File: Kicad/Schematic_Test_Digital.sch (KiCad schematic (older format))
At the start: 71 parts, among them J301 I2C_CONNECTOR_OUT, J302 I2C_CONNECTOR_OUT, J303 CONN_JOYSTICK, J304 I2C_CONNECTOR_OUT, SW301 RESET PUSH, U301 TSX-3225, U302 MMC5603NJ, U303 LSM6DS33TR, U304 74HC595D, U305 74HC595D, U306 74HC595D

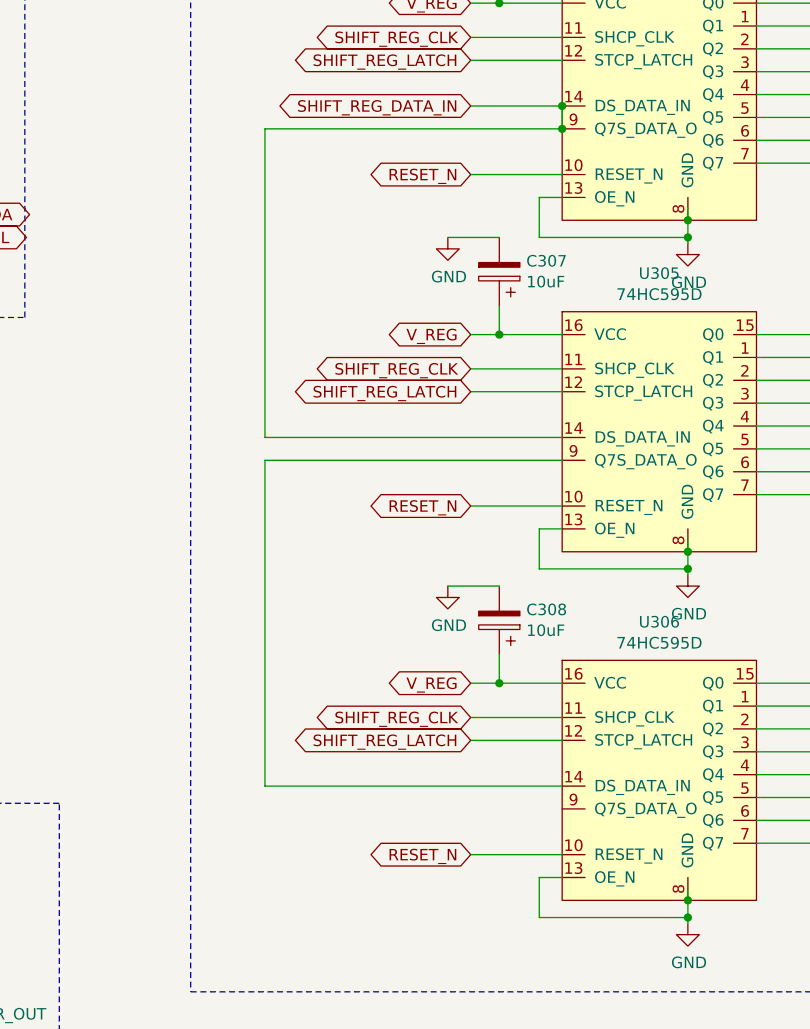
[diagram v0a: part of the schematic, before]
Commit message: Corrected some schematic labeling.
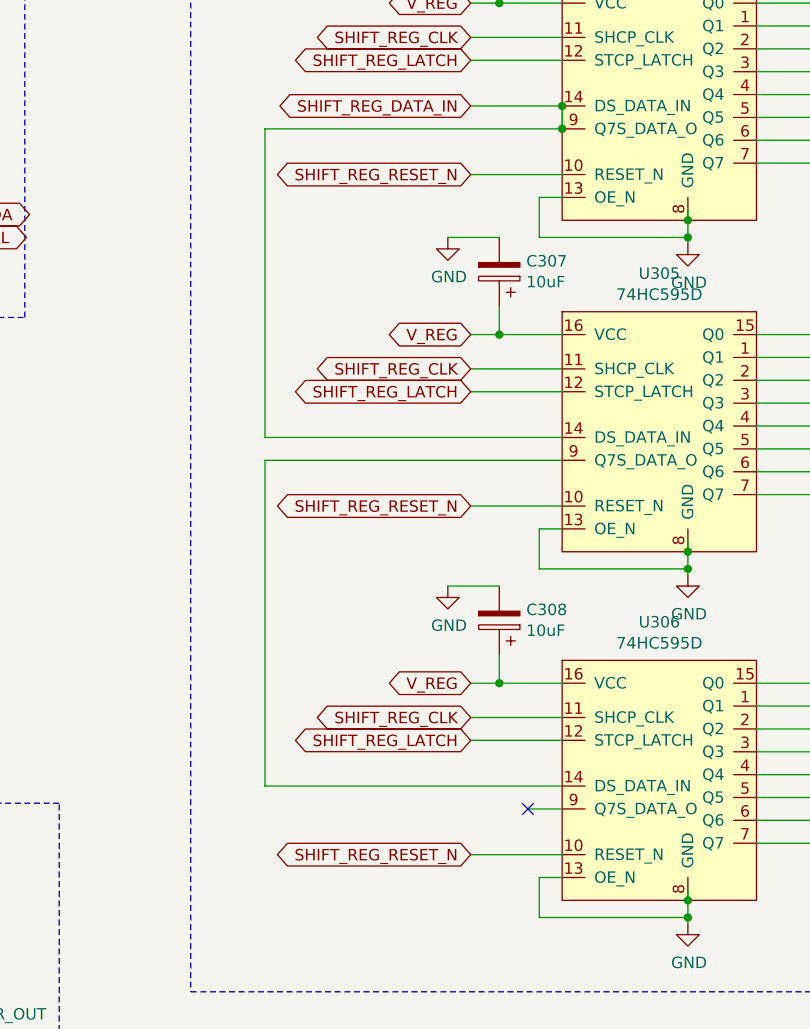
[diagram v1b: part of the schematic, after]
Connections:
- net RESET_N: no longer U304.10 (RESET_N), U305.10 (RESET_N), U306.10 (RESET_N)
- new net SHIFT_REG_RESET_N: U304.10 (RESET_N), U305.10 (RESET_N), U306.10 (RESET_N)
- no-connect marks 2 -> 3
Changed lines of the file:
@@
 Wire Wire Line
 	8700 4950 8300 4950
-Text GLabel 8300 4950 0    50   BiDi ~ 0
-RESET_N
 Wire Wire Line
 	9250 5100 9250 5150
@@
 Wire Wire Line
 	8700 3425 8300 3425
-Text GLabel 8300 3425 0    50   BiDi ~ 0
-RESET_N
 Wire Wire Line
 	9250 3575 9250 3625
@@
 Wire Wire Line
 	8300 1225 8425 1225
-Text GLabel 8300 1975 0    50   BiDi ~ 0
-RESET_N
 Text GLabel 8300 1225 0    50   BiDi ~ 0
 V_REG
@@
 Text GLabel 1800 1375 0    50   BiDi ~ 0
 RESET_N
+Text GLabel 8300 1975 0    50   BiDi ~ 0
+SHIFT_REG_RESET_N
+Text GLabel 8300 3425 0    50   BiDi ~ 0
+SHIFT_REG_RESET_N
+Text GLabel 8300 4950 0    50   BiDi ~ 0
+SHIFT_REG_RESET_N
+Wire Wire Line
+	8700 4750 8550 4750
+NoConn ~ 8550 4750
 $EndSCHEMATC

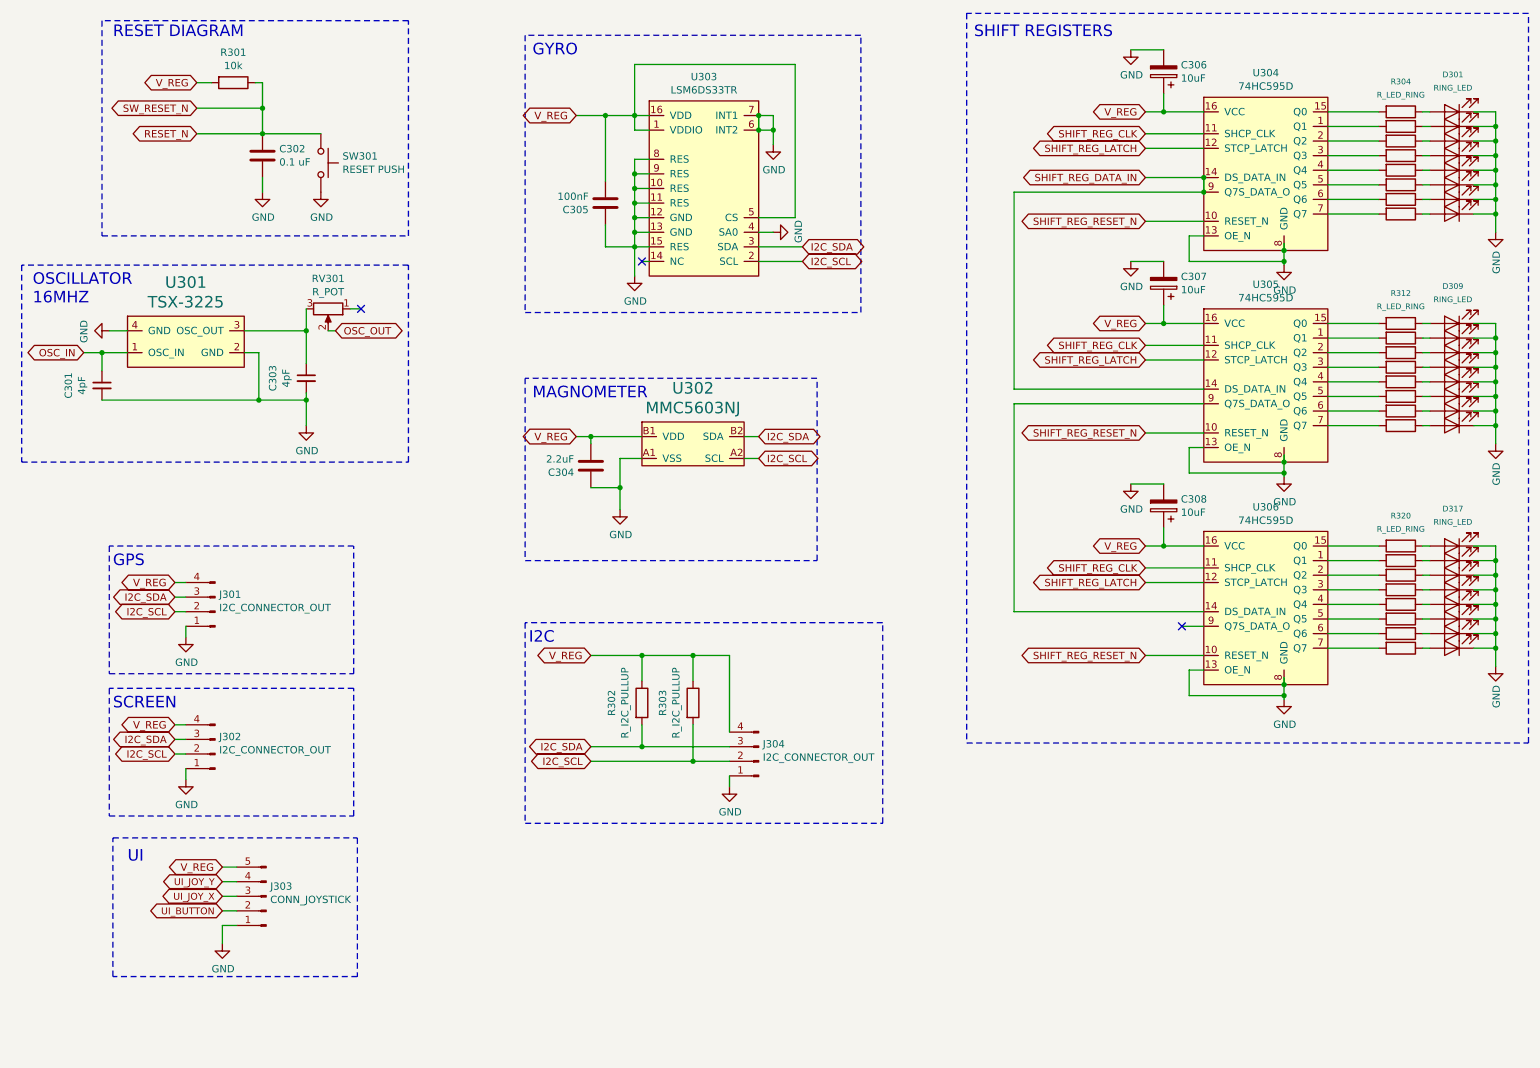
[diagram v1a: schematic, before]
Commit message: Assigned footprints to majority of refs. Missing is i2c due to unknown trace length.
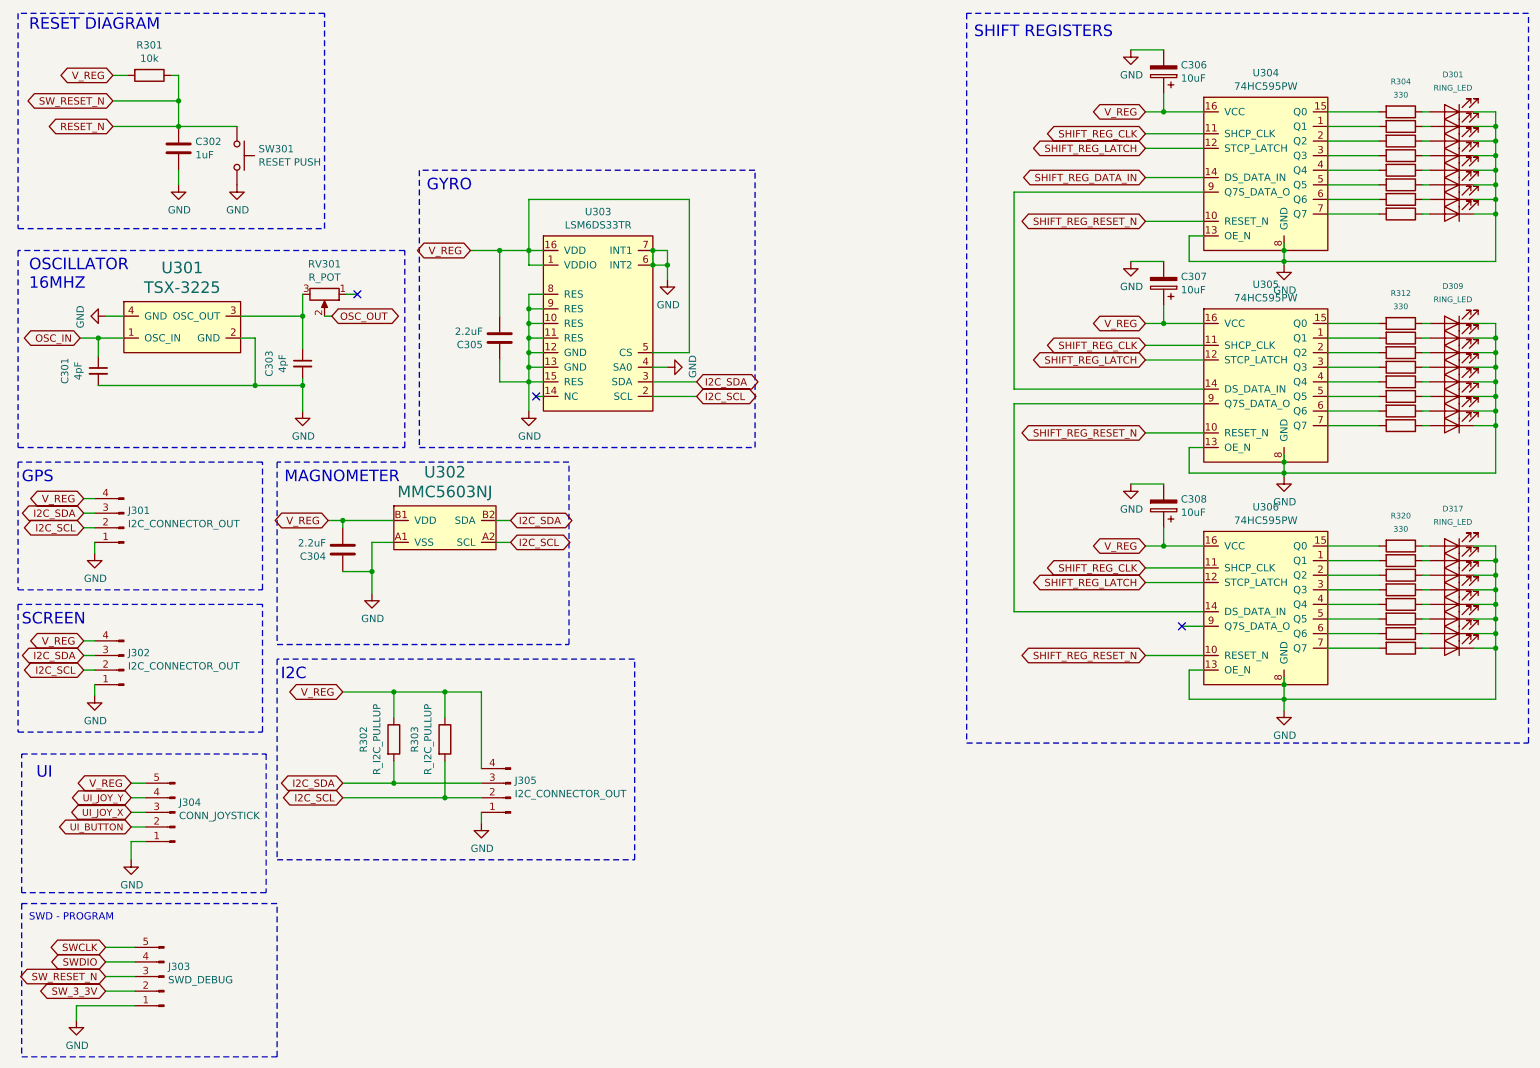
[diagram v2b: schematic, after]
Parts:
- added J303: SWD_DEBUG, Connector_JST:JST_EH_B5B-EH-A_1x05_P2.50mm_Vertical, symbol Connector:Conn_01x05_Male
- C301, C303: footprint (none) -> Capacitor_SMD:C_0805_2012Metric_Pad1.15x1.40mm_HandSolder; part_name (none) -> Capactitor - Crystal; part_url (none) -> https://www.digikey.com/product-detail/en/yageo/CC0805BRNPO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
- C302: value 0.1 uF -> 1uF; footprint (none) -> Capacitor_SMD:C_0805_2012Metric_Pad1.15x1.40mm_HandSolder; part_details part details -> (none); part_name part name example -> Capactitor - Bypass; part_url some.part.url.com -> https://www.digikey.com/product-detail/en/w%C3%BCrth-elektr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
- C304: footprint (none) -> Capacitor_SMD:C_0805_2012Metric_Pad1.15x1.40mm_HandSolder; part_name (none) -> Capactitor - Bypass; part_url (none) -> https://www.digikey.com/product-detail/en/w%C3%BCrth-elektr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
- C305: value 100nF -> 2.2uF; footprint (none) -> Capacitor_SMD:C_0805_2012Metric_Pad1.15x1.40mm_HandSolder; part_name (none) -> Capactitor - Bypass; part_url (none) -> https://www.digikey.com/product-detail/en/w%C3%BCrth-elektr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
- C306, C307, C308: footprint (none) -> Capacitor_SMD:CP_Elec_4x3; part_name (none) -> Capactitor - Bypass; part_url (none) -> https://www.digikey.com/product-detail/en/w%C3%BCrth-elektr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
- D301, D302, D303, D304, D305, D306, D307, D308, D309, D310, D311, D312, D313, D314, D315, D316, D317, D318, D319, D320, D321, D322, D323, D324: footprint (none) -> Diode_SMD:D_1206_3216Metric; part_name (none) -> LED - Green; part_url (none) -> https://www.digikey.com/product-detail/en/w%C3%BCrth-elektr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
- J301, J302: footprint (none) -> Connector_JST:JST_EH_B4B-EH-A_1x04_P2.50mm_Vertical; part_details (none) -> JST - 4 pin; part_url (none) -> LOCAL STOCK
- J304: renamed from J303; footprint (none) -> Connector_JST:JST_EH_B5B-EH-A_1x05_P2.50mm_Vertical; part_details (none) -> JST - 5 pin; part_url (none) -> LOCAL STOCK
- J305: renamed from J304; footprint (none) -> Connector_JST:JST_EH_B4B-EH-A_1x04_P2.50mm_Vertical; part_details (none) -> JST - 4 pin; part_url (none) -> LOCAL STOCK
- R302, R303: footprint (none) -> Resistor_SMD:R_1206_3216Metric_Pad1.42x1.75mm_HandSolder
- R304, R305, R306, R307, R308, R309, R310, R311, R312, R313, R314, R315, R316, R317, R318, R319, R320, R321, R322, R323, R324, R325, R326, R327: value R_LED_RING -> 330; footprint (none) -> Resistor_SMD:R_1206_3216Metric_Pad1.42x1.75mm_HandSolder; part_details (none) -> Limits current to 8mA; part_name (none) -> Resistor - LED Ring; part_url (none) -> https://www.digikey.com/product-detail/en/yageo/RC1206FR-07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
- SW301: footprint (none) -> Button_Switch_SMD:SW_SPST_CK_RS282G05A3; part_name (none) -> Push Switch; part_url (none) -> https://www.digikey.com/product-detail/en/c-k/PTS636-SM43-S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
- U301: footprint Kicad:TSX-3225 -> Crystal:Crystal_SMD_SeikoEpson_TSX3225-4Pin_3.2x2.5mm_HandSoldering
- U302: footprint (none) -> Package_BGA:WLP-4_0.73x0.73mm_Layout2x2_P0.35mm_Ball0.22mm_Pad0.2mm_NSMD
- U304, U305, U306: value 74HC595D -> 74HC595PW; footprint Kicad:StarGazer_74HC595D_SOIC-16 -> Package_SO:TSSOP-14_4.4x5mm_P0.65mm; part_name 74HC595D,118 -> 74HC595PW,118; part_url https://www.digikey.com/product-detail/en/nexperia-usa-inc/74HC595D-118/1727-2821-1-ND/763394 -> https://www.digikey.com/product-detail/en/nexperia-usa-inc/74HC595PW-112/1727-6439-ND/1230493
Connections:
- net GND: now also J303.1 (Pin_1)
- net RESET_N: now also J303.3 (Pin_3)
- net SHIFT_REG_DATA_IN: no longer U304.9 (Q7S_DATA_O), U305.14 (DS_DATA_IN)
- new net: U304.9 (Q7S_DATA_O), U305.14 (DS_DATA_IN)
- new net SWCLK: J303.5 (Pin_5)
- new net SWDIO: J303.4 (Pin_4)
- new net SW_3_3V: J303.2 (Pin_2)
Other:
- note added: "SWD - PROGRAM\n"
- moved on the sheet: C301, C302, C303, C304, C305, J301, J302, J304, J305, R301, R302, R303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

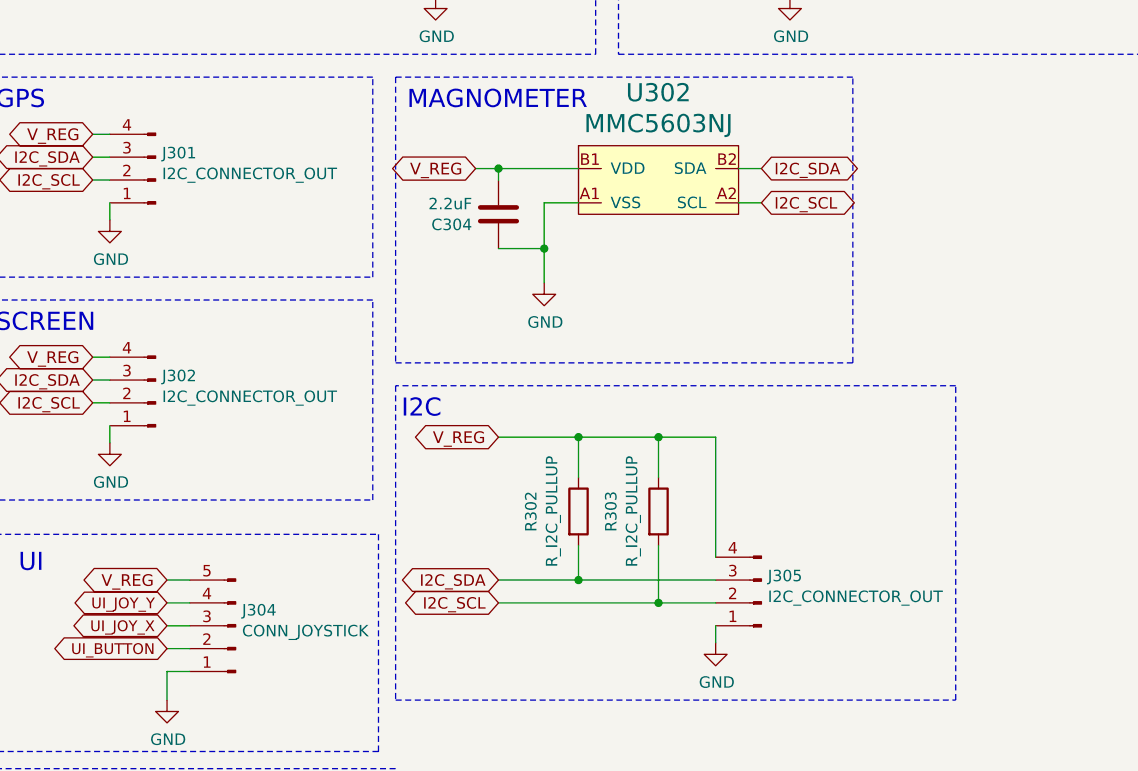
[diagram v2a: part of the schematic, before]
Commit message: Continued (slow) devolopment.
PCB board has begun.  Parts are pushed out to where they need to roughly be.
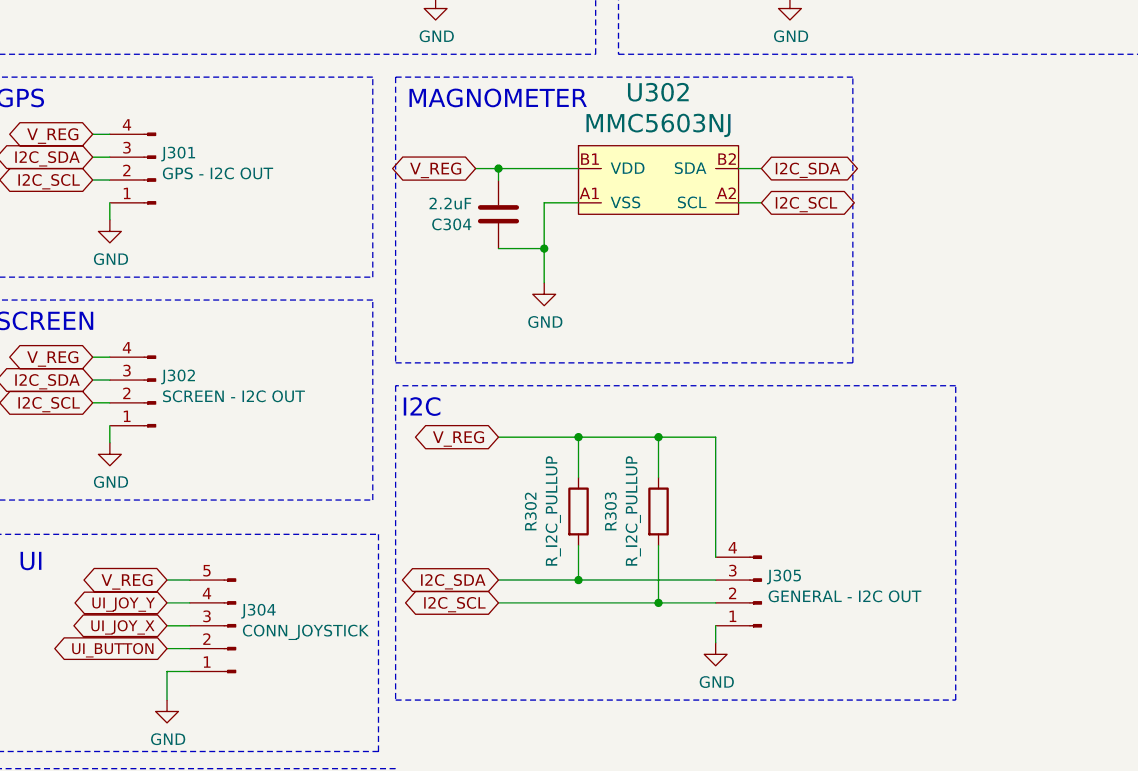
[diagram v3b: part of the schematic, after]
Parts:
- J301: value I2C_CONNECTOR_OUT -> GPS - I2C OUT; part_url LOCAL STOCK -> (none)
- J302: value I2C_CONNECTOR_OUT -> SCREEN - I2C OUT; part_url LOCAL STOCK -> (none)
- J305: value I2C_CONNECTOR_OUT -> GENERAL - I2C OUT; part_url LOCAL STOCK -> (none)
- U304, U305, U306: footprint Package_SO:TSSOP-14_4.4x5mm_P0.65mm -> Package_SO:TSSOP-16_4.4x5mm_P0.65mm
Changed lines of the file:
@@
 AR Path="/5F580392/5F64B2DD" Ref="J302"  Part="1"
 F 0 "J302" H 1272 4932 50  0000 R CNN
-F 1 "I2C_CONNECTOR_OUT" H 1272 5023 50  0000 R CNN
+F 1 "SCREEN - I2C OUT" H 1272 5023 50  0000 R CNN
 F 2 "Connector_JST:JST_EH_B4B-EH-A_1x04_P2.50mm_Vertical" H 1300 5050 50  0001 C CNN
 F 3 "~" H 1300 5050 50  0001 C CNN
 F 4 "JST - 4 pin" H 1300 5050 50  0001 C CNN "part_details"
-F 5 "LOCAL STOCK" H 1300 5050 50  0001 C CNN "part_url"
+F 5 "" H 1300 5050 50  0001 C CNN "part_url"
 	1    1300 5050
 	-1   0    0    1
@@
 AR Path="/5F580392/5F64B2F5" Ref="J301"  Part="1"
 F 0 "J301" H 1272 3957 50  0000 R CNN
-F 1 "I2C_CONNECTOR_OUT" H 1272 4048 50  0000 R CNN
+F 1 "GPS - I2C OUT" H 1272 4048 50  0000 R CNN
 F 2 "Connector_JST:JST_EH_B4B-EH-A_1x04_P2.50mm_Vertical" H 1300 4075 50  0001 C CNN
 F 3 "~" H 1300 4075 50  0001 C CNN
 F 4 "JST - 4 pin" H 1300 4075 50  0001 C CNN "part_details"
-F 5 "LOCAL STOCK" H 1300 4075 50  0001 C CNN "part_url"
+F 5 "" H 1300 4075 50  0001 C CNN "part_url"
 	1    1300 4075
 	-1   0    0    1
@@
 	0    1    1    0
 $EndComp
-Wire Wire Line
-	9550 4200 9900 4200
 Connection ~ 10700 3375
 Wire Wire Line
@@
 AR Path="/5F580392/5F64B4A9" Ref="J305"  Part="1"
 F 0 "J305" H 3922 5807 50  0000 R CNN
-F 1 "I2C_CONNECTOR_OUT" H 3922 5898 50  0000 R CNN
+F 1 "GENERAL - I2C OUT" H 3922 5898 50  0000 R CNN
 F 2 "Connector_JST:JST_EH_B4B-EH-A_1x04_P2.50mm_Vertical" H 3950 5925 50  0001 C CNN
 F 3 "~" H 3950 5925 50  0001 C CNN
 F 4 "JST - 4 pin" H 3950 5925 50  0001 C CNN "part_details"
-F 5 "LOCAL STOCK" H 3950 5925 50  0001 C CNN "part_url"
+F 5 "" H 3950 5925 50  0001 C CNN "part_url"
 	1    3950 5925
 	-1   0    0    1
@@
 	3000 4375 3000 4525
 Connection ~ 3000 4375
-Wire Wire Line
-	2800 4025 3150 4025
-Connection ~ 2800 4025
 Wire Wire Line
 	2700 4025 2800 4025
@@
 	1    0    0    -1
 $EndComp
-Wire Wire Line
-	3150 4175 3000 4175
-Wire Wire Line
-	3950 4175 3850 4175
-Wire Wire Line
-	3950 4025 3850 4025
 $Comp
 L StarGazer:MMC5603NJ U?
@@
 F 0 "U304" H 9125 1092 50  0000 C CNN
 F 1 "74HC595PW" H 9125 1000 51  0000 C CNN
-F 2 "Package_SO:TSSOP-14_4.4x5mm_P0.65mm" H 9200 1125 50  0001 C CNN
+F 2 "Package_SO:TSSOP-16_4.4x5mm_P0.65mm" H 9200 1125 50  0001 C CNN
 F 3 "" H 9200 1125 50  0001 C CNN
 F 4 "Shift Register" H 9150 1025 50  0001 C CNN "part_details"
@@
 F 0 "U306" H 9125 4067 50  0000 C CNN
 F 1 "74HC595PW" H 9125 3975 51  0000 C CNN
-F 2 "Package_SO:TSSOP-14_4.4x5mm_P0.65mm" H 9200 4100 50  0001 C CNN
+F 2 "Package_SO:TSSOP-16_4.4x5mm_P0.65mm" H 9200 4100 50  0001 C CNN
 F 3 "" H 9200 4100 50  0001 C CNN
 F 4 "Shift Register" H 9150 4000 50  0001 C CNN "part_details"
@@
 F 0 "U305" H 9125 2542 50  0000 C CNN
 F 1 "74HC595PW" H 9125 2450 51  0000 C CNN
-F 2 "Package_SO:TSSOP-14_4.4x5mm_P0.65mm" H 9200 2575 50  0001 C CNN
+F 2 "Package_SO:TSSOP-16_4.4x5mm_P0.65mm" H 9200 2575 50  0001 C CNN
 F 3 "" H 9200 2575 50  0001 C CNN
 F 4 "Shift Register" H 9150 2475 50  0001 C CNN "part_details"
@@
 Text Notes 650  6775 0    50   ~ 0
 SWD - PROGRAM\n
+Wire Wire Line
+	9550 4200 9900 4200
+Wire Wire Line
+	2800 4025 3150 4025
+Connection ~ 2800 4025
+Wire Wire Line
+	3000 4175 3150 4175
+Wire Wire Line
+	3950 4175 3850 4175
+Wire Wire Line
+	3850 4025 3950 4025
 $EndSCHEMATC
